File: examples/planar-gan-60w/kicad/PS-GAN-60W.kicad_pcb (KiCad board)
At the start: 8 copper layers, 64 x 56 mm, 89 parts, among them J1 48 V INPUT, J2 12 V / 5 A, Q1 CSD18543Q3A, Q2 CSD18543Q3A, T1 4 : 2 : 2 / ELP22, U1 LMG2100R044, U2 UCC25600, U3 UCC24624, U4 LM5164, U5 TPS7A2450, U6 EL357N, U7 TL431A, U8 EL357N, U9 TL431A

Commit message: Improve GaN reference planes and output distribution from layout review
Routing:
- net VOUT: track 145.9 -> 121.8 mm, vias 14 -> 18
- net AGND: track 30.1 -> 16.5 mm, vias 30 -> 31
- net SGND: track 16.6 -> 19.2 mm, vias 42 -> 48
- net PGND: vias 59 -> 57
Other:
- board text added: "PS-GAN-60W / A8"
- board text removed: "PS-GAN-60W / A7"

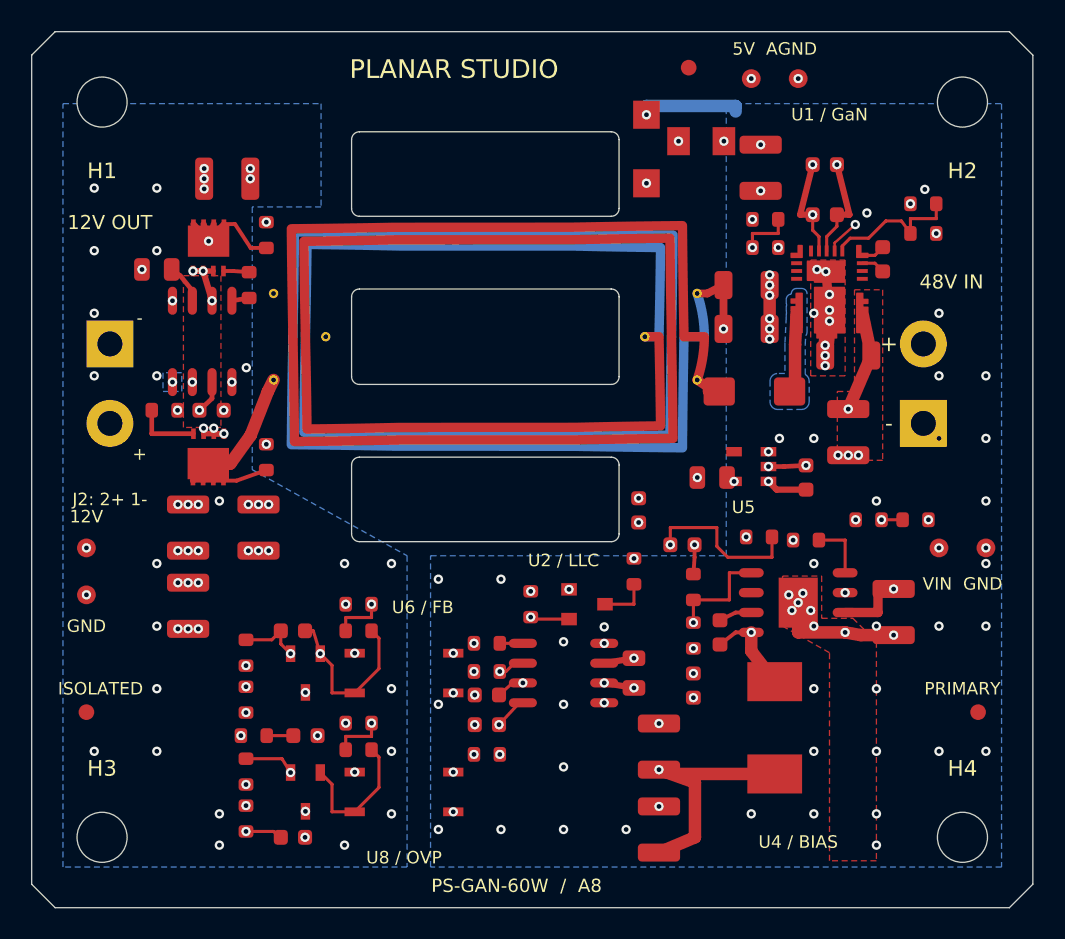
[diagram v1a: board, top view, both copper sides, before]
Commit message: Repair GaN manufacturing geometry and purposeful copper pours (A11)
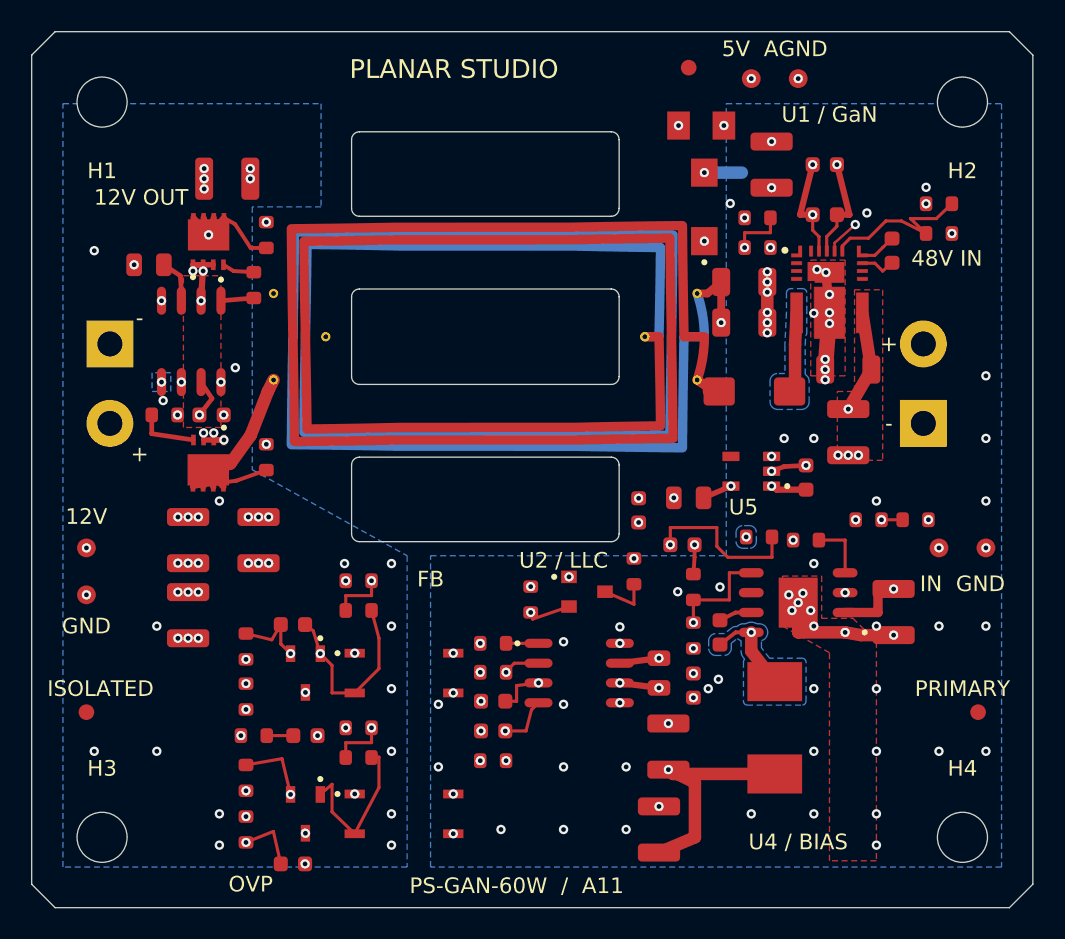
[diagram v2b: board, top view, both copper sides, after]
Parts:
- moved D1 5.23 mm to (96.0, 67.2)
- moved C26 1.98 mm to (95.0, 85.8)
- moved C29 1.70 mm to (69.7, 109.2)
- moved C10 1.60 mm to (93.1, 97.0)
- moved R20 1.50 mm to (73.9, 91.1)
- moved U8 1.40 mm to (76.8, 106.0)
- moved U9 1.40 mm to (70.5, 106.0)
- moved R21 1.30 mm to (73.9, 93.0)
- moved F1 1.00 mm to (95.8, 62.0)
- moved R4 1.00 mm to (111.0, 67.0)
- moved R5 1.00 mm to (111.0, 68.9)
- moved U2 1.00 mm to (88.0, 97.0)
- moved C3 0.90 mm to (105.2, 77.6)
- moved C4 0.81 mm to (108.0, 70.0)
- moved C13 0.80 mm to (63.0, 88.5)
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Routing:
- net /SS: track 8.66 -> 13.6 mm
- net VIN: track 85.6 -> 90.5 mm
- net Net-(U9-REF): track 10.9 -> 14.4 mm
- net VOUT: track 121.8 -> 125.1 mm
- net PGND: track 34.2 -> 31.1 mm, vias 57 -> 53
- net /VIN_RAW: track 39.9 -> 37.0 mm
- net V5: track 61.1 -> 63.3 mm
- net BIAS12: track 95.6 -> 93.7 mm
- net /HI: track 9.30 -> 10.9 mm
- net Net-(D2-C): track 9.06 -> 10.7 mm
- net Net-(U6-AN): track 7.24 -> 8.82 mm
- net SGND: track 19.2 -> 20.7 mm, vias 48 -> 42
- net Net-(U8-CA): track 9.08 -> 10.5 mm
- net Net-(U6-CA): track 20.8 -> 22.1 mm
- net Net-(U2-RT): track 7.55 -> 8.81 mm
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- added copper zone on In6.Cu, net /VIN_RAW
- added copper zone on In4.Cu, net VOUT
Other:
- board text added: "FB"
- board text added: "IN GND"
- board text added: "OVP"
- board text added: "PS-GAN-60W / A11"
- board text removed: "J2: 2+ 1-"
- board text removed: "PS-GAN-60W / A8"
- board text removed: "U6 / FB"
- board text removed: "U8 / OVP"
- board text removed: "VIN GND"

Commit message: Clean GaN routing and silkscreen; supply single-board A12 files
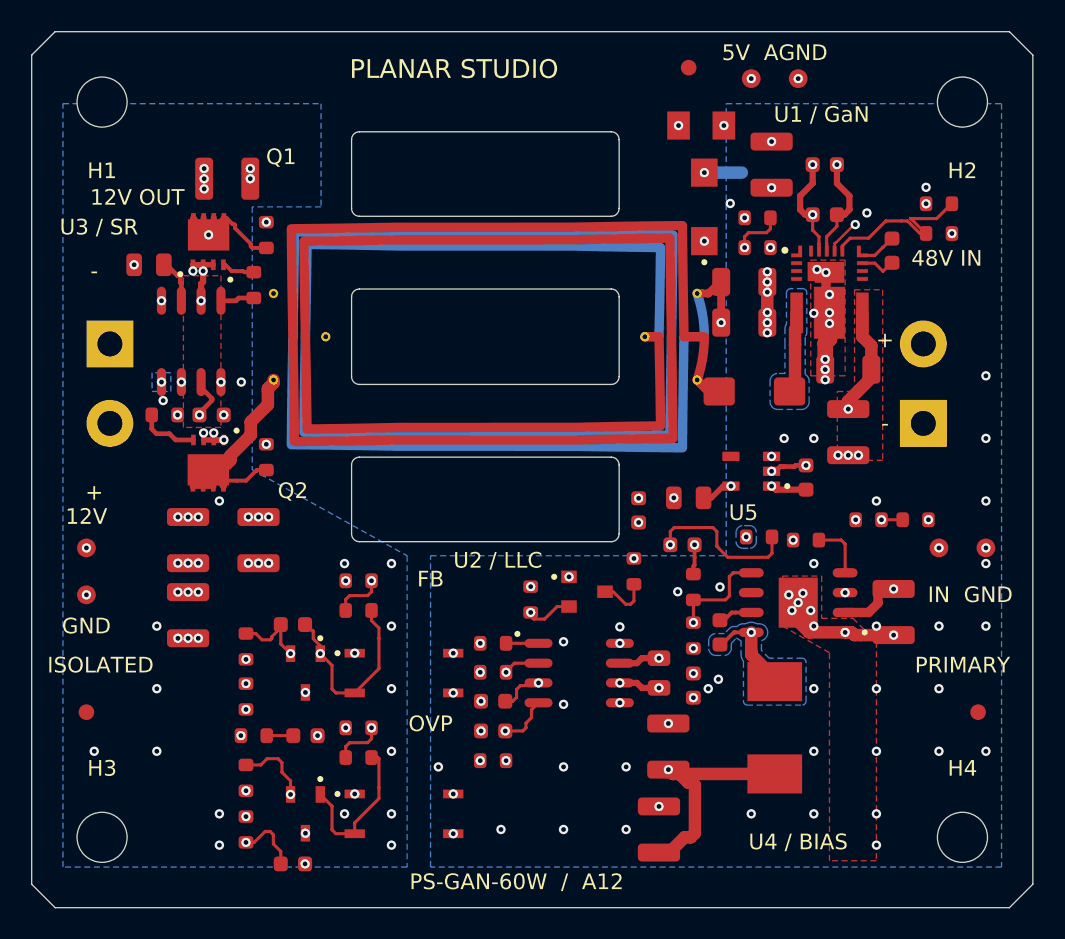
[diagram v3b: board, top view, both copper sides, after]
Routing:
- net VOUT: track 125.1 -> 123.4 mm
- net /VIN_RAW: track 37.0 -> 35.4 mm
- net Net-(T1-S_END): track 17.6 -> 18.5 mm
- net VIN: track 90.5 -> 89.7 mm
- net AGND: track 17.0 -> 17.5 mm, vias 33 -> 32
- net BIAS12: track 93.7 -> 93.2 mm
- net PGND: track 31.1 -> 31.0 mm, vias 53 -> 55
- net SGND: track 20.7 -> 20.8 mm, vias 42 -> 43
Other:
- board text added: "PS-GAN-60W / A12"
- board text added: "Q1"
- board text added: "Q2"
- board text added: "U3 / SR"
- board text removed: "PS-GAN-60W / A11"

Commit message: Rework GaN feedback placement and direct pad-to-pad routing (A13)
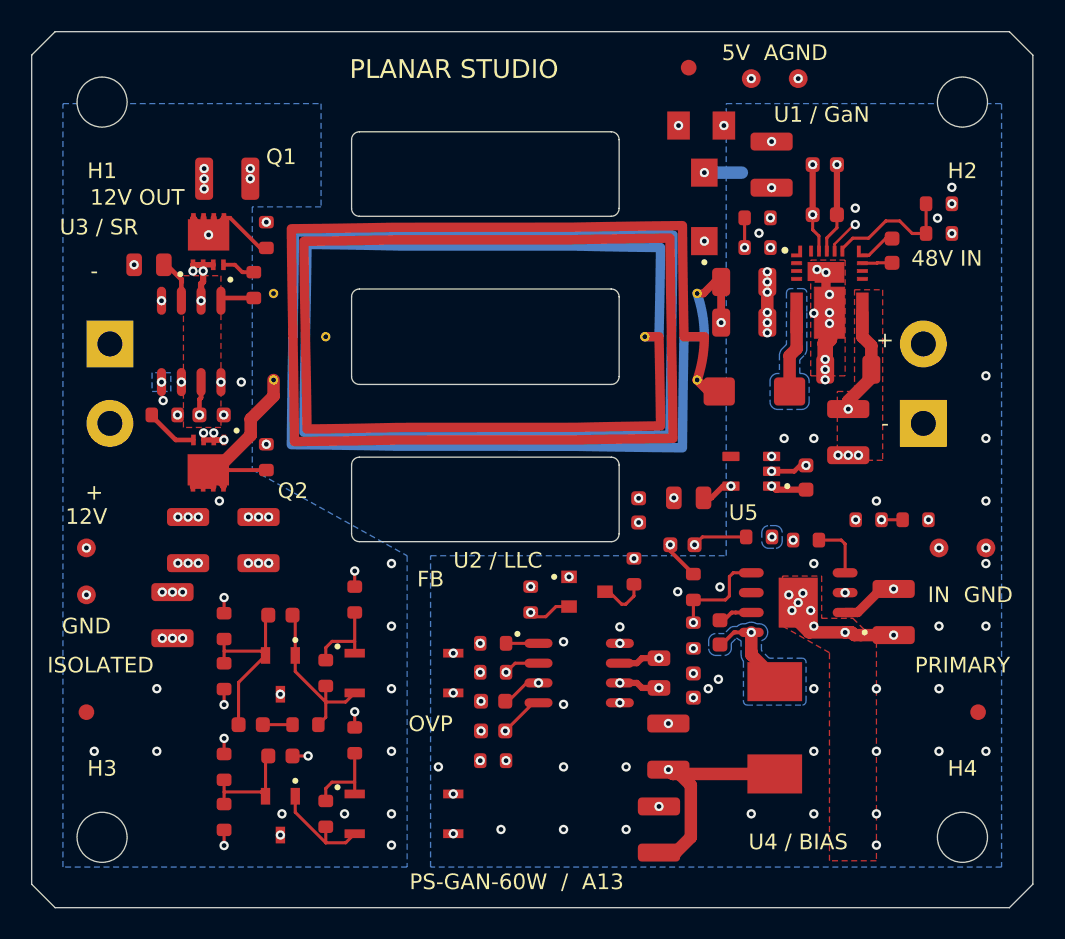
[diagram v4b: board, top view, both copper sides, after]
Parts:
- moved C29 6.95 mm to (68.9, 102.3)
- moved R21 4.52 mm to (71.8, 97.0), turned to -90 degrees
- moved R26 4.17 mm to (71.8, 106.0), turned to -90 degrees
- moved C27 3.57 mm to (67.0, 100.3), turned to 180 degrees
- moved R24 3.37 mm to (70.5, 100.3), turned to 180 degrees
- moved R22 1.91 mm to (65.3, 94.0), turned to -90 degrees
- moved R23 1.91 mm to (65.3, 97.2), turned to -90 degrees
- moved R28 1.61 mm to (65.3, 106.2), turned to -90 degrees
- moved U7 1.60 mm to (68.9, 97.1)
- moved U9 1.60 mm to (68.9, 106.1)
- moved R27 1.57 mm to (65.3, 103.0), turned to -90 degrees
- moved R20 1.23 mm to (73.7, 92.3), turned to -90 degrees
- moved C28 1.00 mm to (68.9, 93.3)
- moved C16 1.00 mm to (62.0, 93.3)
- moved R25 0.84 mm to (73.7, 101.3), turned to -90 degrees
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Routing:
- net Net-(U6-CA): track 22.2 -> 11.2 mm, vias 2 -> 0
- net Net-(U9-REF): track 14.1 -> 6.96 mm, vias 2 -> 0
- net Net-(C23-Pad1): track 21.0 -> 14.9 mm
- net Net-(U7-REF): track 15.8 -> 12.1 mm, vias 3 -> 0
- net Net-(U6-AN): track 8.64 -> 5.42 mm, vias 2 -> 0
- net VIN: track 89.7 -> 86.5 mm
- net Net-(U8-CA): track 10.1 -> 6.90 mm
- net Net-(U8-AN): track 8.38 -> 5.42 mm, vias 2 -> 0
- net SGND: track 20.8 -> 23.7 mm, vias 43 -> 40
- net BIAS12: track 93.2 -> 90.6 mm
- net /HI: track 11.1 -> 8.47 mm
- net /LI: track 14.5 -> 12.6 mm
- net /VIN_RAW: track 35.4 -> 33.7 mm
- net V5: track 62.8 -> 61.4 mm
- net Net-(U2-GD2): track 40.5 -> 41.7 mm
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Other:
- board text added: "PS-GAN-60W / A13"
- board text removed: "PS-GAN-60W / A12"

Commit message: Audit JLC turnkey readiness and shorten rectifier gate routing (A14)
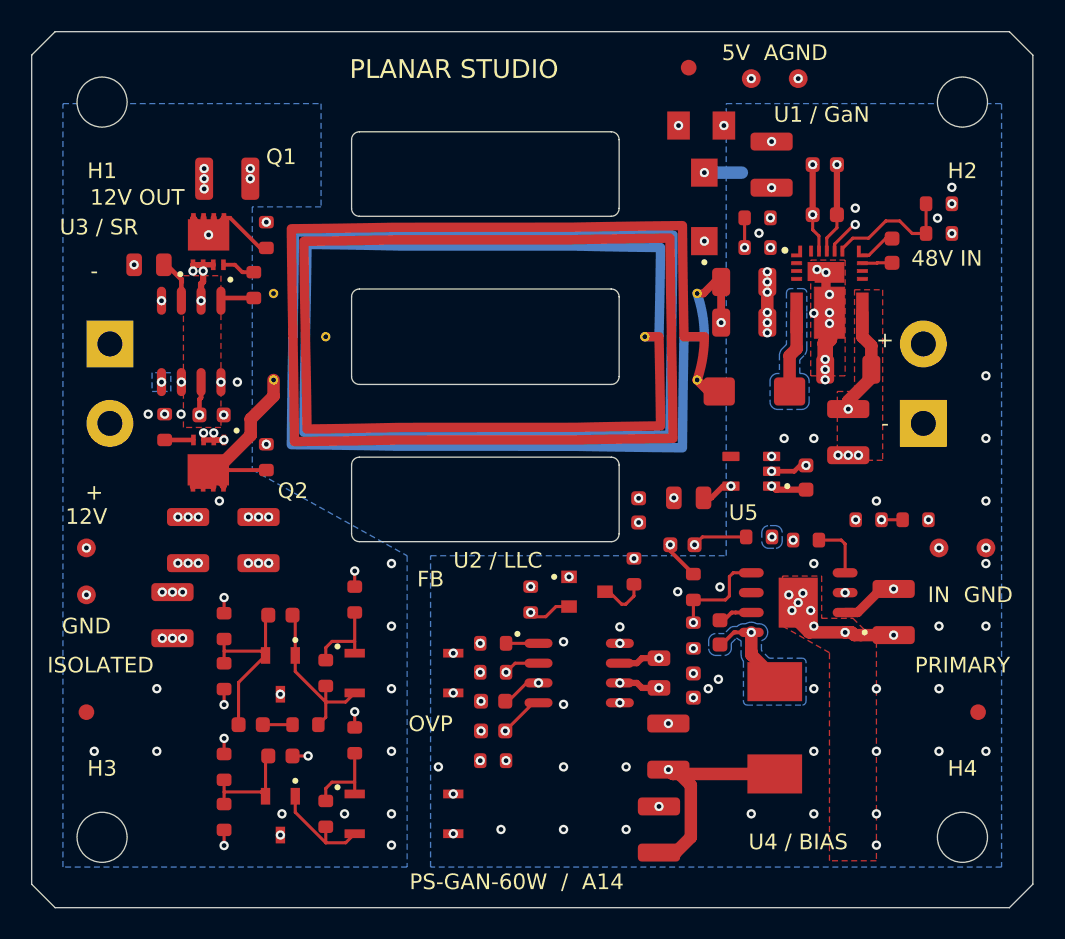
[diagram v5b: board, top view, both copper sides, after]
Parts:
- moved R11 0.78 mm to (61.5, 81.3), turned to -90 degrees
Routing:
- net Net-(U3-VG2): track 6.83 -> 4.45 mm
- net Net-(Q2-G): track 3.37 -> 1.84 mm
- net SGND: track 23.7 -> 24.4 mm, vias 40 -> 41
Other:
- board text added: "PS-GAN-60W / A14"
- board text removed: "PS-GAN-60W / A13"
